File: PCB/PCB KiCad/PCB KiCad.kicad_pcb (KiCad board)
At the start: 2 copper layers, 80 x 120 mm, 73 parts, among them J1 ADC Debug, J2 LED Debug, J3 Qwiic, SW1 MCU_RESET, SW2 TRIGGER, U1 OPA2376xxD, U2 ADS1256IDBT, U3 LM285D-2.5, U4 AMS1117-3.3, U5 TLC59208FIPWR, Y1 7.68MHz

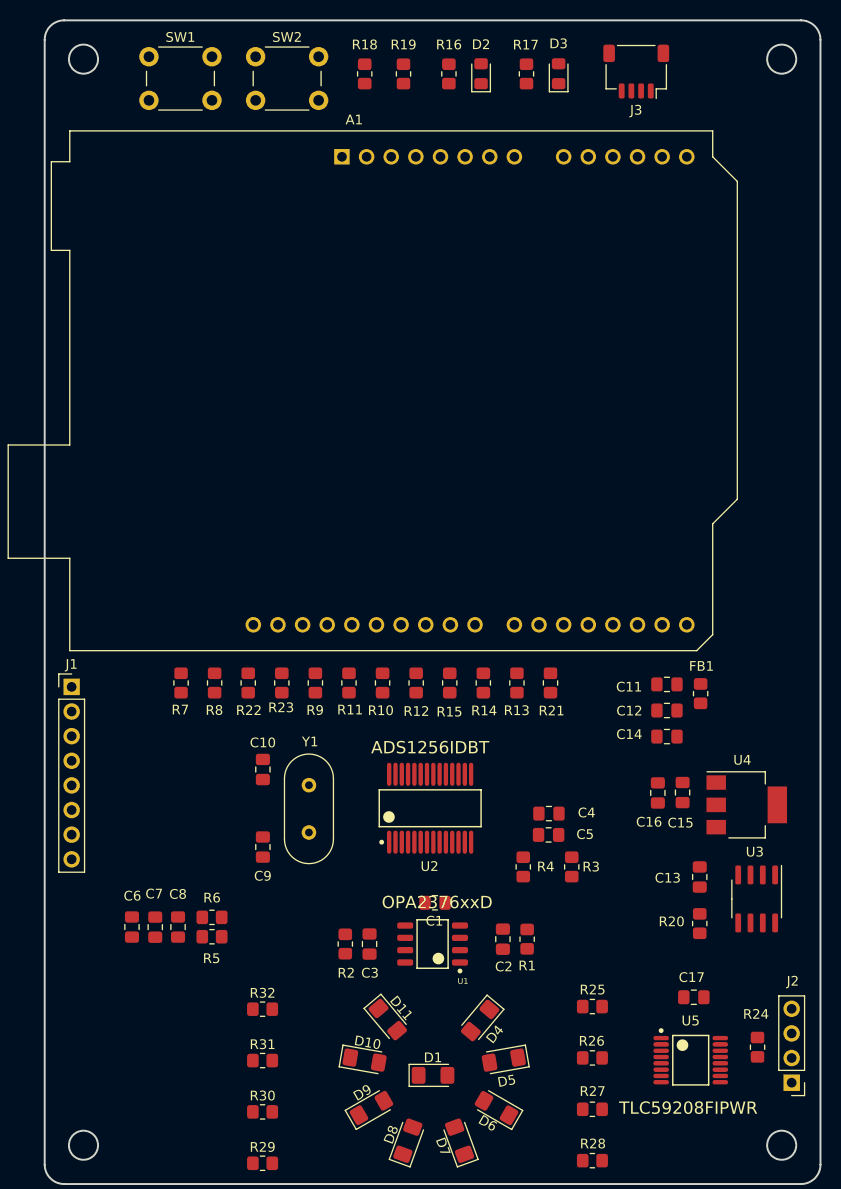
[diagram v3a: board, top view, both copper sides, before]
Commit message: placement: rough layout done
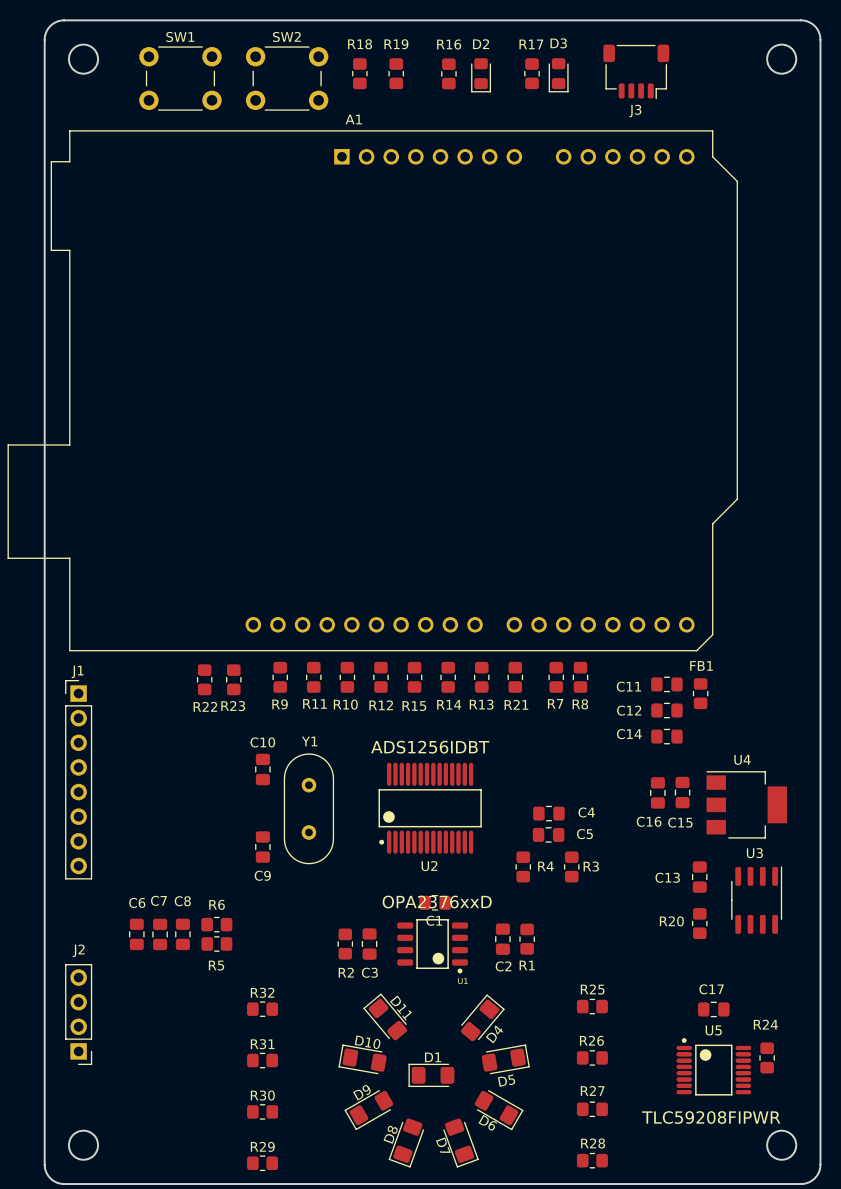
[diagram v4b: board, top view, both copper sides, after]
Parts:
- moved J2 73.6 mm to (46.5, 134.3)
- moved R7 38.7 mm to (95.8, 95.8)
- moved R8 37.7 mm to (98.2, 95.8)
- moved R23 4.96 mm to (62.5, 96.0)
- moved R22 4.50 mm to (59.5, 96.0)
- moved R10 3.67 mm to (74.2, 95.8)
- moved R11 3.67 mm to (70.8, 95.8)
- moved R12 3.67 mm to (77.7, 95.8)
- moved R13 3.67 mm to (88.1, 95.8)
- moved R14 3.67 mm to (84.6, 95.8)
- moved R15 3.67 mm to (81.1, 95.8)
- moved R21 3.67 mm to (91.5, 95.8)
- moved R9 3.67 mm to (67.3, 95.8)
- moved U5 2.59 mm to (112.0, 136.2)
- moved C17 2.41 mm to (112.0, 130.0)
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
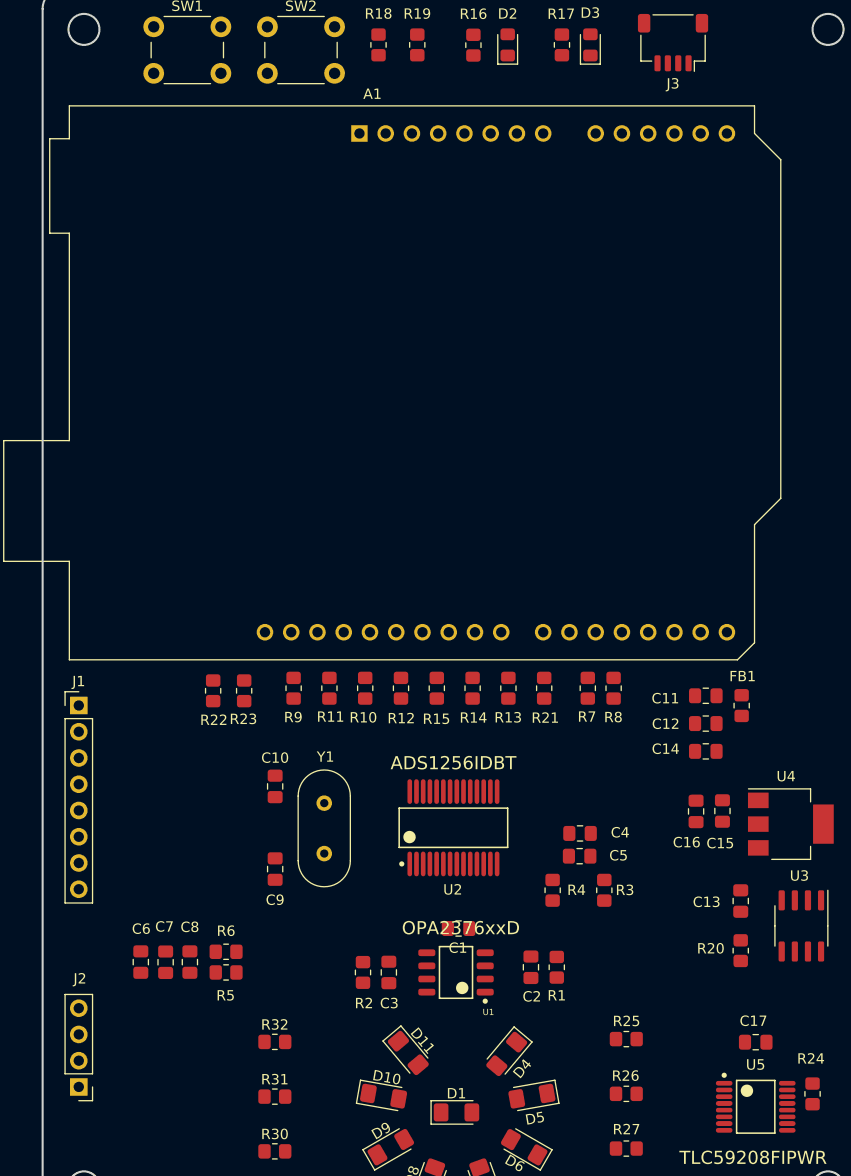
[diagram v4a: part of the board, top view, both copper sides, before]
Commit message: routing: high-speed and sensitive signal routing done
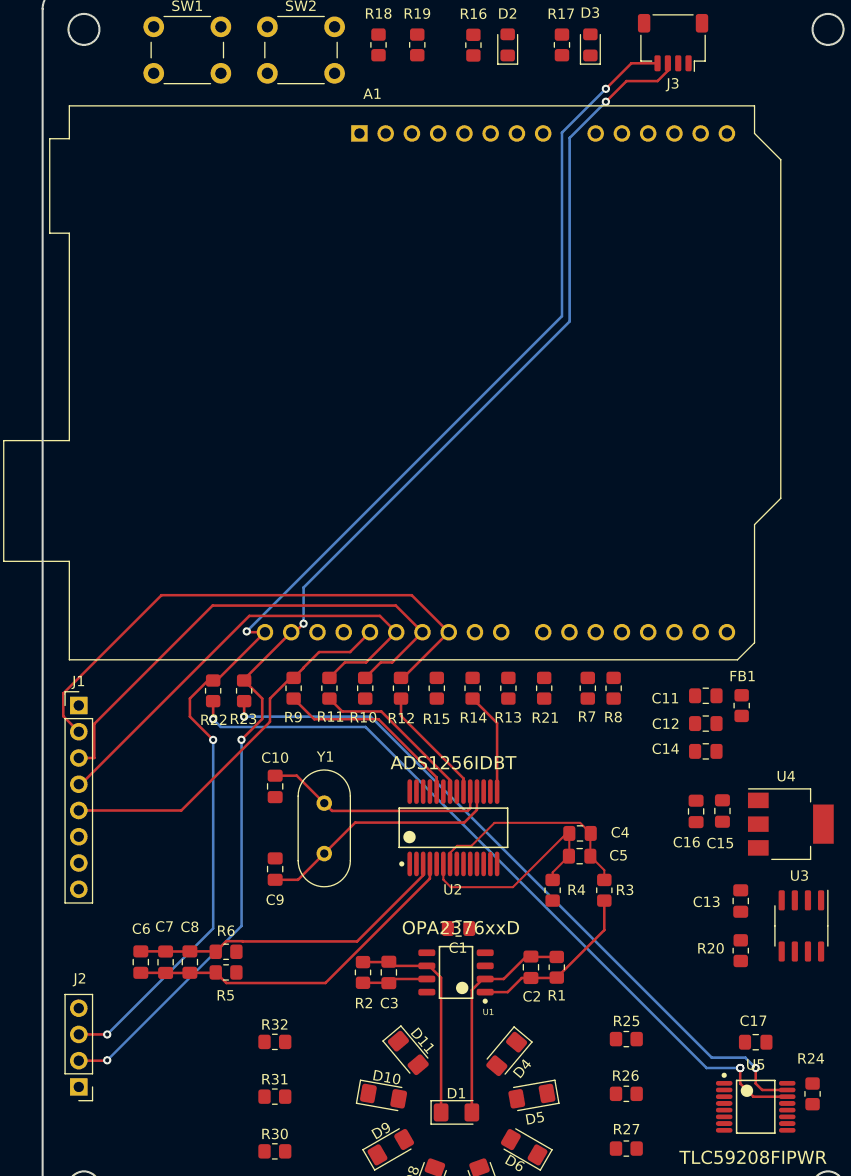
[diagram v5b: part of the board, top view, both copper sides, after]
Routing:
- net /LED/I2C.SDA: track 0.00 -> 125.3 mm, vias 0 -> 4
- net /LED/I2C.SCL: track 0.00 -> 125.1 mm, vias 0 -> 4
- net Net-(R22-Pad2): track 0.00 -> 73.3 mm, vias 0 -> 3
- net Net-(R23-Pad2): track 0.00 -> 69.9 mm, vias 0 -> 2
- net /ADC/SPI.CS: track 0.00 -> 53.5 mm
- net /ADC/SPI.MOSI: track 0.00 -> 49.7 mm
- net /ADC/SPI.MISO: track 0.00 -> 46.4 mm
- net /ADC/SPI.CLK: track 0.00 -> 36.7 mm
- net Net-(C6-Pad1): track 0.00 -> 34.0 mm
- net Net-(C6-Pad2): track 0.00 -> 31.5 mm
- net Net-(C9-Pad2): track 0.00 -> 24.1 mm
- net /ADC/AIN+: track 0.00 -> 22.4 mm
- net Net-(C10-Pad1): track 0.00 -> 22.0 mm
- net Net-(C2-Pad1): track 0.00 -> 21.4 mm
- net /ADC/AIN-: track 0.00 -> 21.4 mm
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
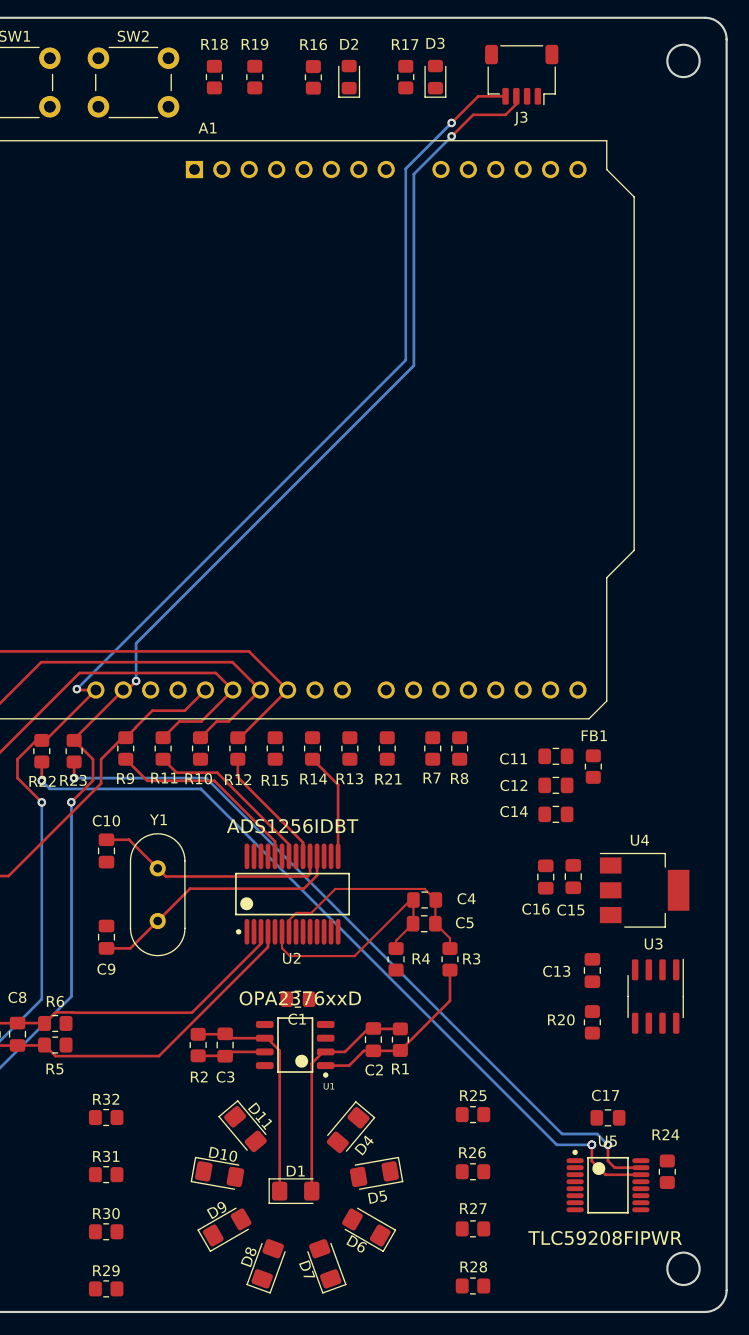
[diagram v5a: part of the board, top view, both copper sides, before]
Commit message: routing: power pins connected
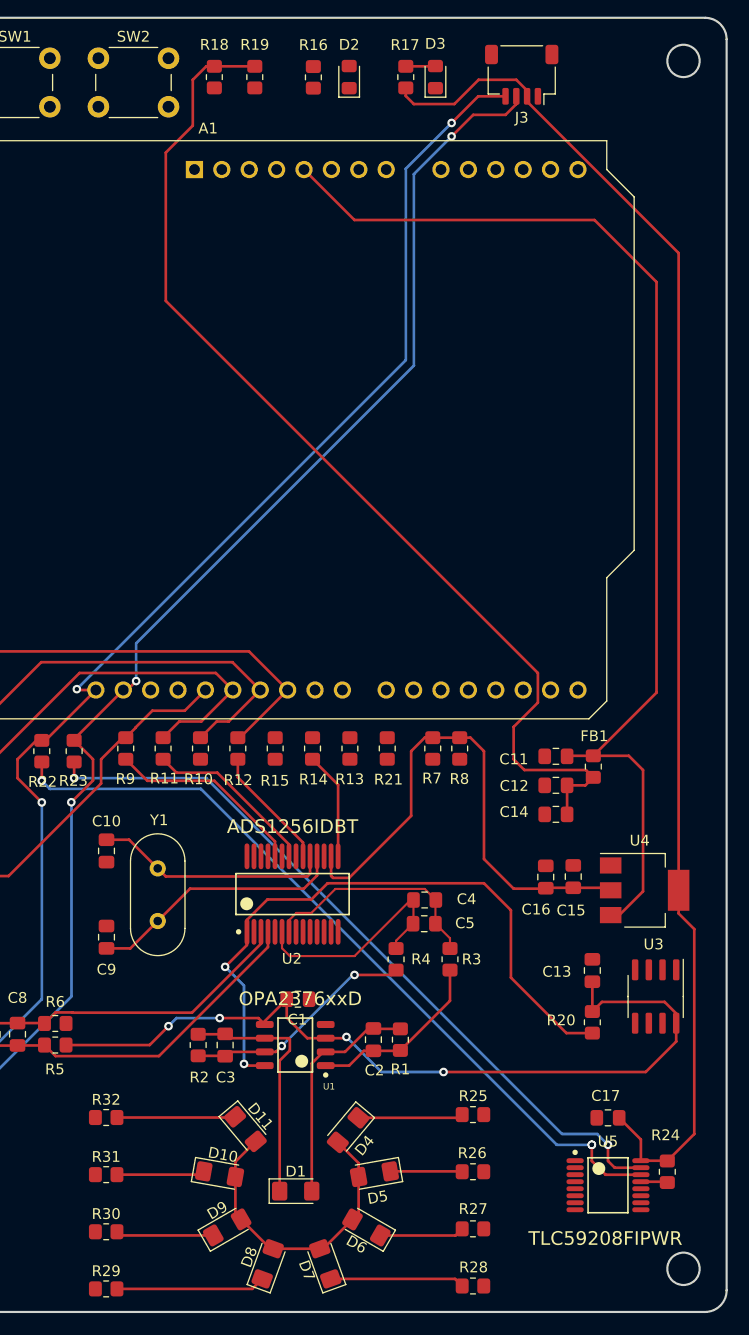
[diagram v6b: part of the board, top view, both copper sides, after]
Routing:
- net +3V3: track 0.00 -> 205.3 mm
- net +5V: track 0.00 -> 158.8 mm, vias 0 -> 2
- net /MCU + IO/+5V RAW: track 0.00 -> 106.1 mm
- net +2V5: track 0.00 -> 78.1 mm, vias 0 -> 4
- net Net-(C3-Pad2): track 6.76 -> 22.1 mm, vias 0 -> 2
- net Net-(D8-Pad1): track 0.00 -> 13.9 mm
- net Net-(D7-Pad1): track 0.00 -> 12.5 mm
- net Net-(D11-Pad1): track 0.00 -> 11.0 mm
- net Net-(D4-Pad1): track 0.00 -> 9.74 mm
- net Net-(D9-Pad1): track 0.00 -> 9.07 mm
- net Net-(D10-Pad1): track 0.00 -> 8.18 mm
- net Net-(D6-Pad1): track 0.00 -> 7.85 mm
- net Net-(D5-Pad1): track 0.00 -> 6.69 mm
- net Net-(D3-Pad2): track 0.00 -> 2.76 mm
- net Net-(R21-Pad2): track 0.00 -> 2.48 mm
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
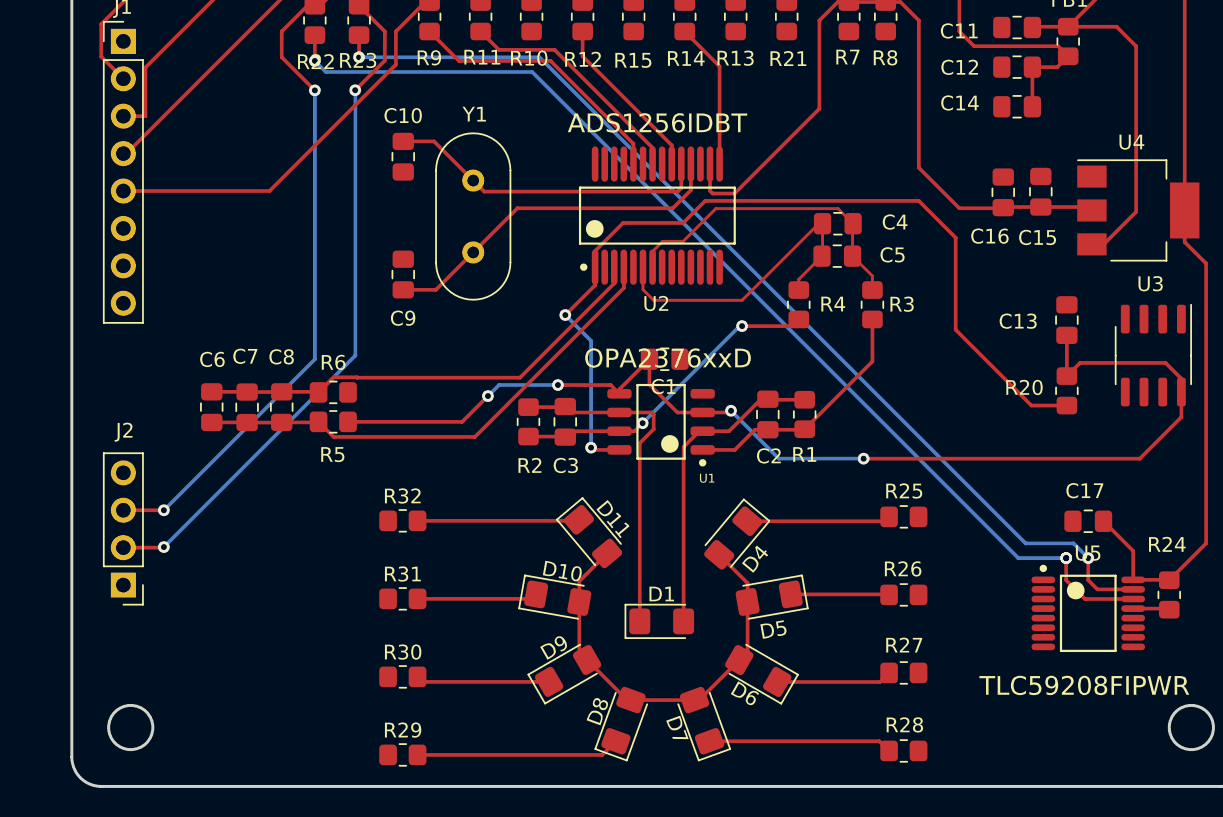
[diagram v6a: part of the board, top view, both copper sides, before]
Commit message: routing: fix J2 orientation (more intuitive)
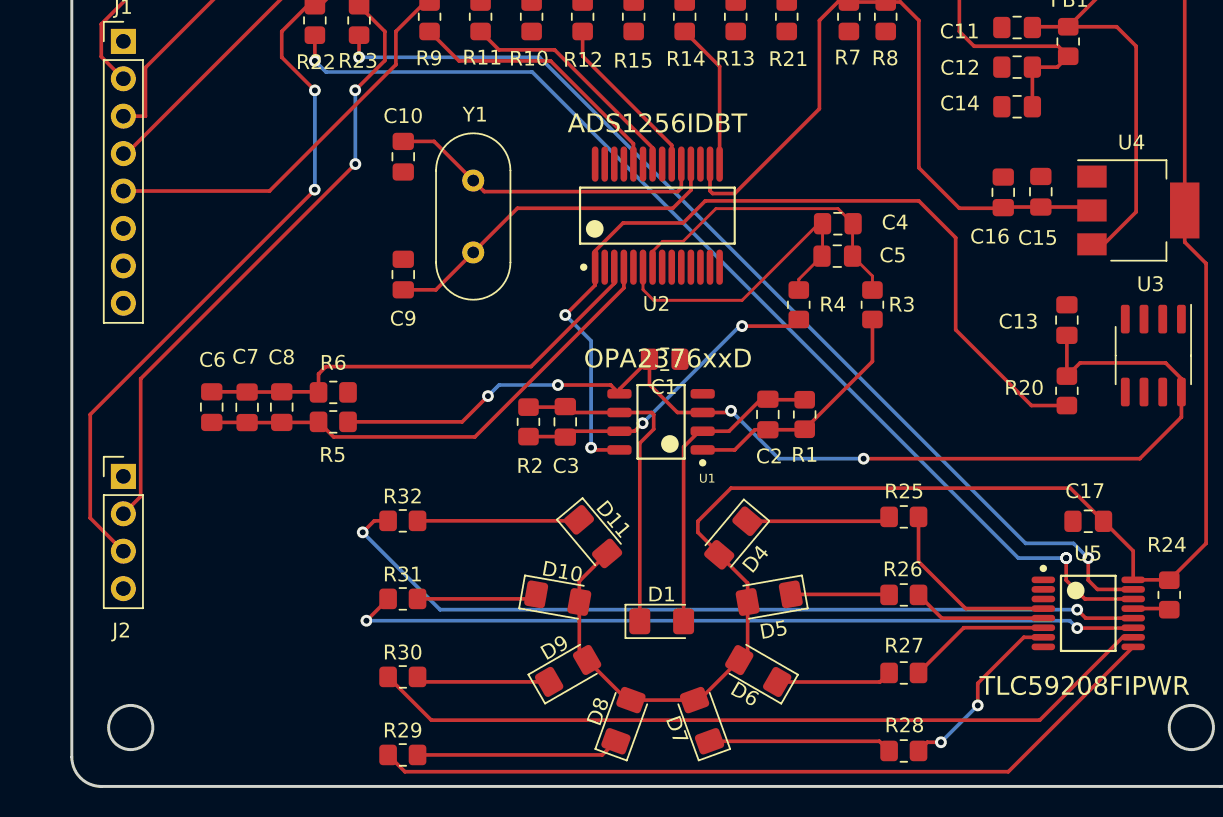
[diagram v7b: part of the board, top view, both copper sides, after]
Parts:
- moved J2 7.38 mm to (46.5, 127.0), turned to 0 degrees
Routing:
- net Net-(R32-Pad1): track 0.00 -> 56.8 mm, vias 0 -> 2
- net Net-(R29-Pad1): track 0.00 -> 54.6 mm
- net Net-(R31-Pad1): track 0.00 -> 54.4 mm, vias 0 -> 2
- net Net-(R30-Pad1): track 0.00 -> 54.1 mm
- net +3V3: track 205.3 -> 237.6 mm
- net Net-(R25-Pad1): track 0.00 -> 12.8 mm
- net Net-(R28-Pad1): track 0.00 -> 12.5 mm, vias 0 -> 2
- net Net-(R27-Pad1): track 0.00 -> 9.74 mm
- net Net-(R26-Pad1): track 0.00 -> 9.12 mm
- net /LED/I2C.SDA: track 125.3 -> 121.4 mm
- net /LED/I2C.SCL: track 125.1 -> 128.1 mm
- net Net-(C6-Pad2): track 31.5 -> 32.2 mm
